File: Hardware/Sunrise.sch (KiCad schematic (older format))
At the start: 8 parts, among them U1 LM3401, U2 HC-06

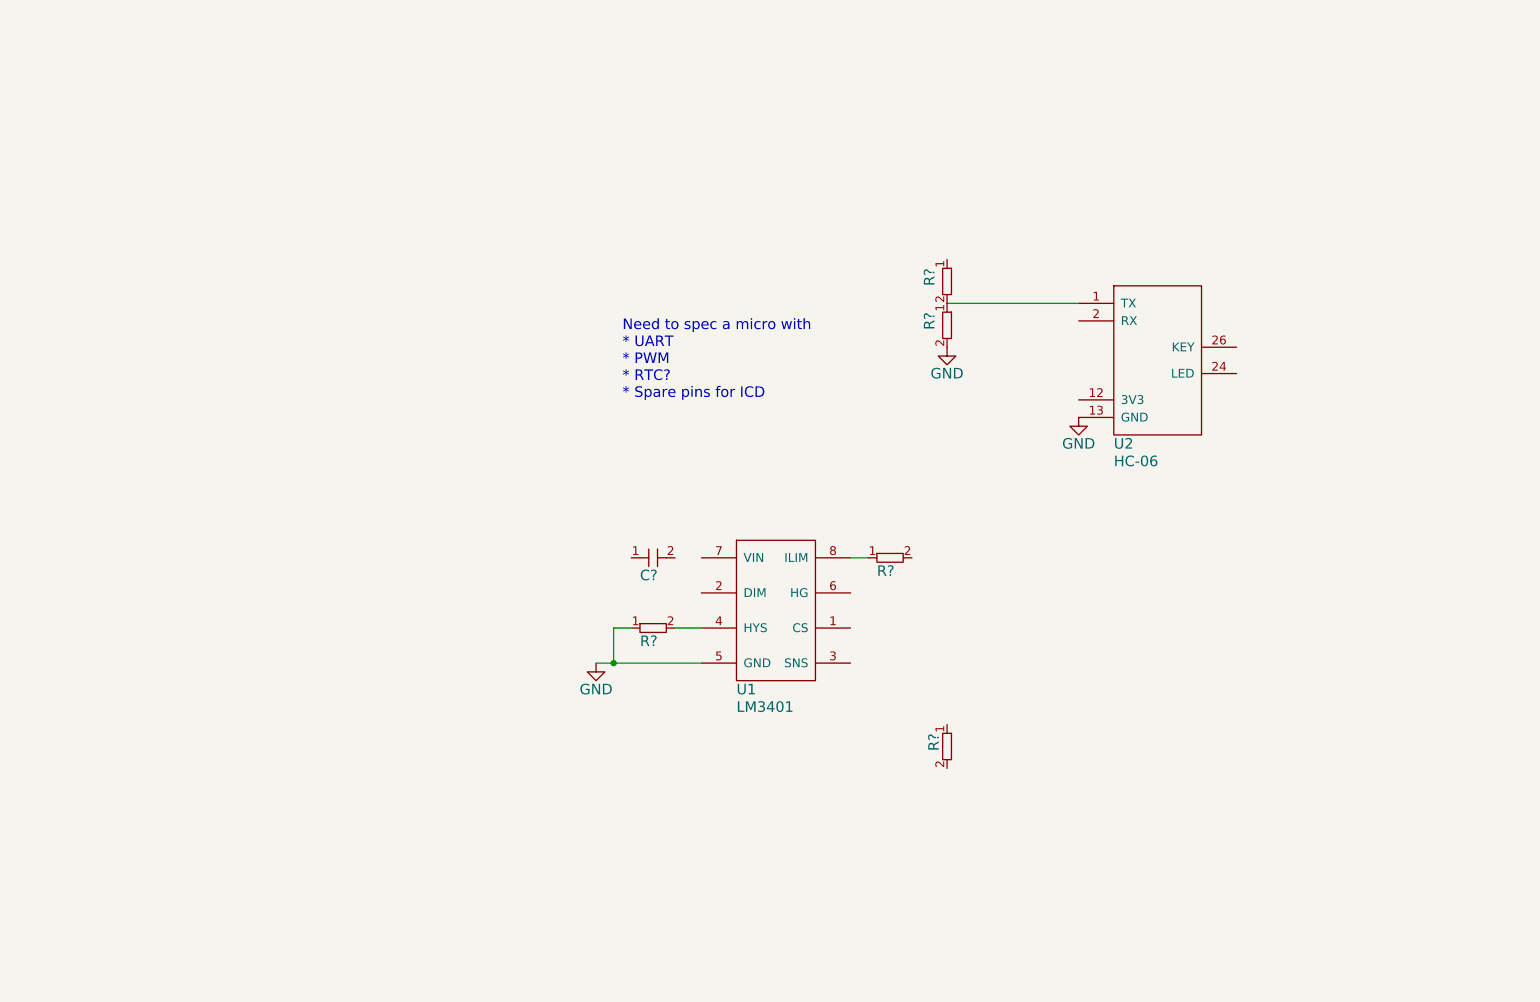
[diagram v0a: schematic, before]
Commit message: LED part of schematic drawn
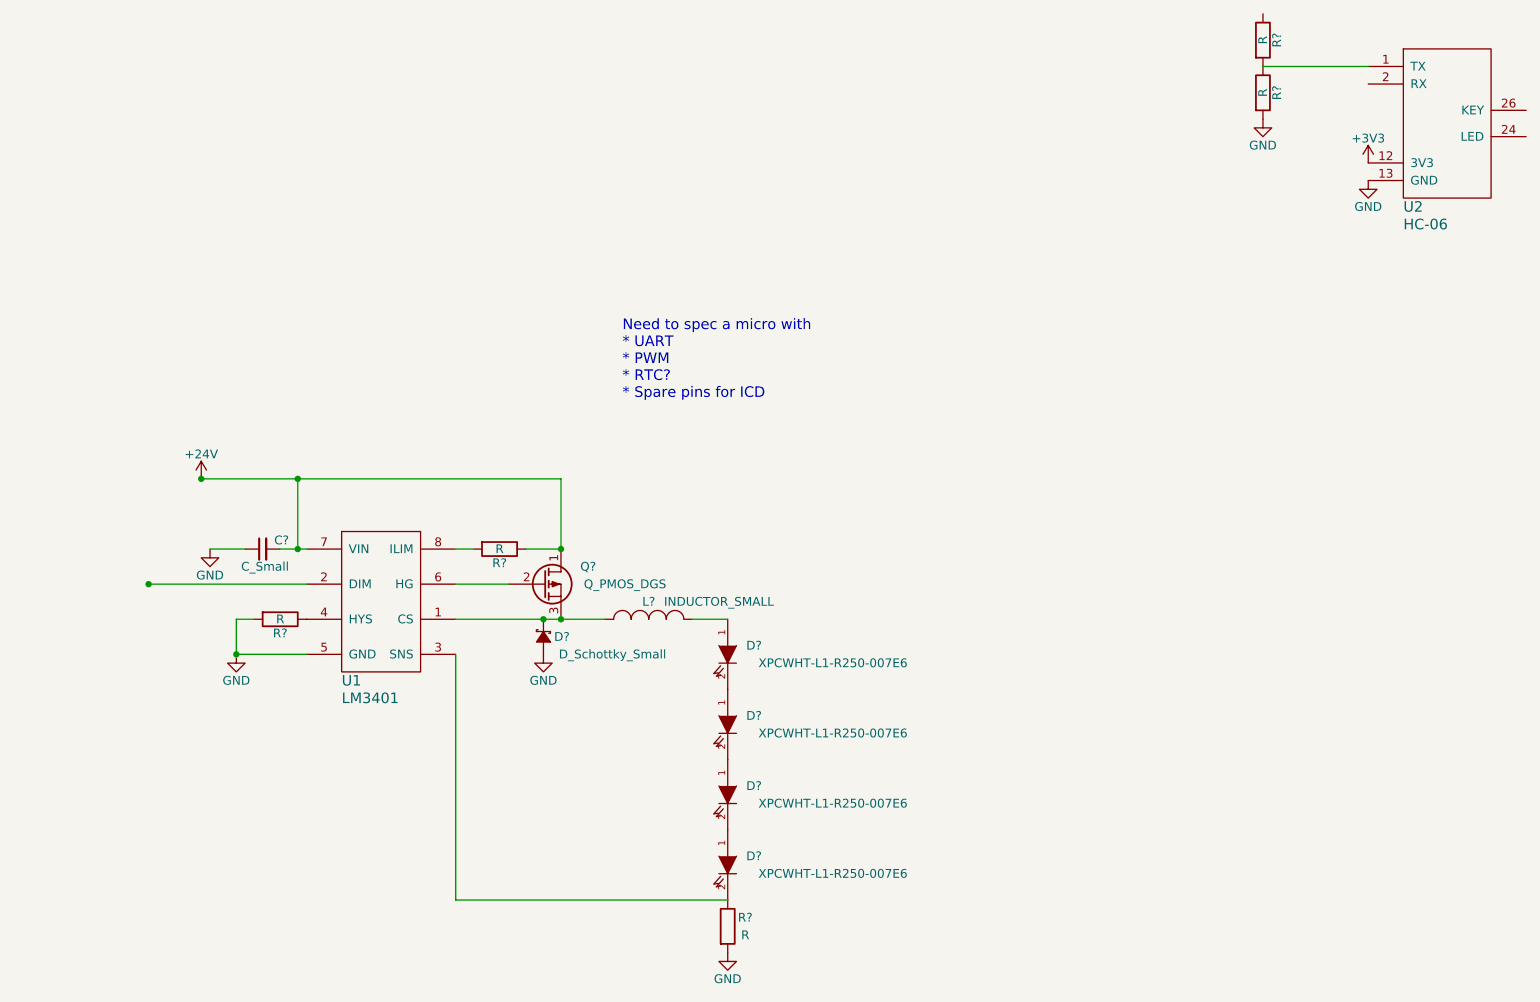
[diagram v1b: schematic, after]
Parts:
- removed C?: Cap, symbol Cap
- removed R? (x5): Resistor, symbol Resistor
- added C?: C_Small, symbol C_Small
- added D?: D_Schottky_Small, symbol D_Schottky_Small
- added D? (x4): XPCWHT-L1-R250-007E6, symbol LED
- added L?: INDUCTOR_SMALL, symbol INDUCTOR_SMALL
- added Q?: Q_PMOS_DGS, symbol Q_PMOS_DGS
- added R? (x5): R, symbol R
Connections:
- net GND: now also C?.1, D?.1 (A), R?.2, R?.2, R?.2
- net at U2.1 (TX): now also R?.1, R?.2
- net +3V3: now reaches U2.12 (3V3)
- net at U1.1 (CS): now also D?.2 (C), L?.1, Q?.3 (S)
- net at U1.3 (SNS): now also D?.2 (K), R?.1
- net at U1.4 (HYS): now also R?.1
- net at U1.6 (HG): now also Q?.2 (G)
- net +24V: now reaches U1.7 (VIN)
- net +24V: now also C?.2, Q?.1 (D), R?.1
- net at U1.8 (ILIM): now also R?.2
- new net: D?.1 (A), L?.2
- new net: D?.1 (A), D?.2 (K) (x3)
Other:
- moved on the sheet: U1, U2

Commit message: Added detail to schematic. Started LED driver calcs in python
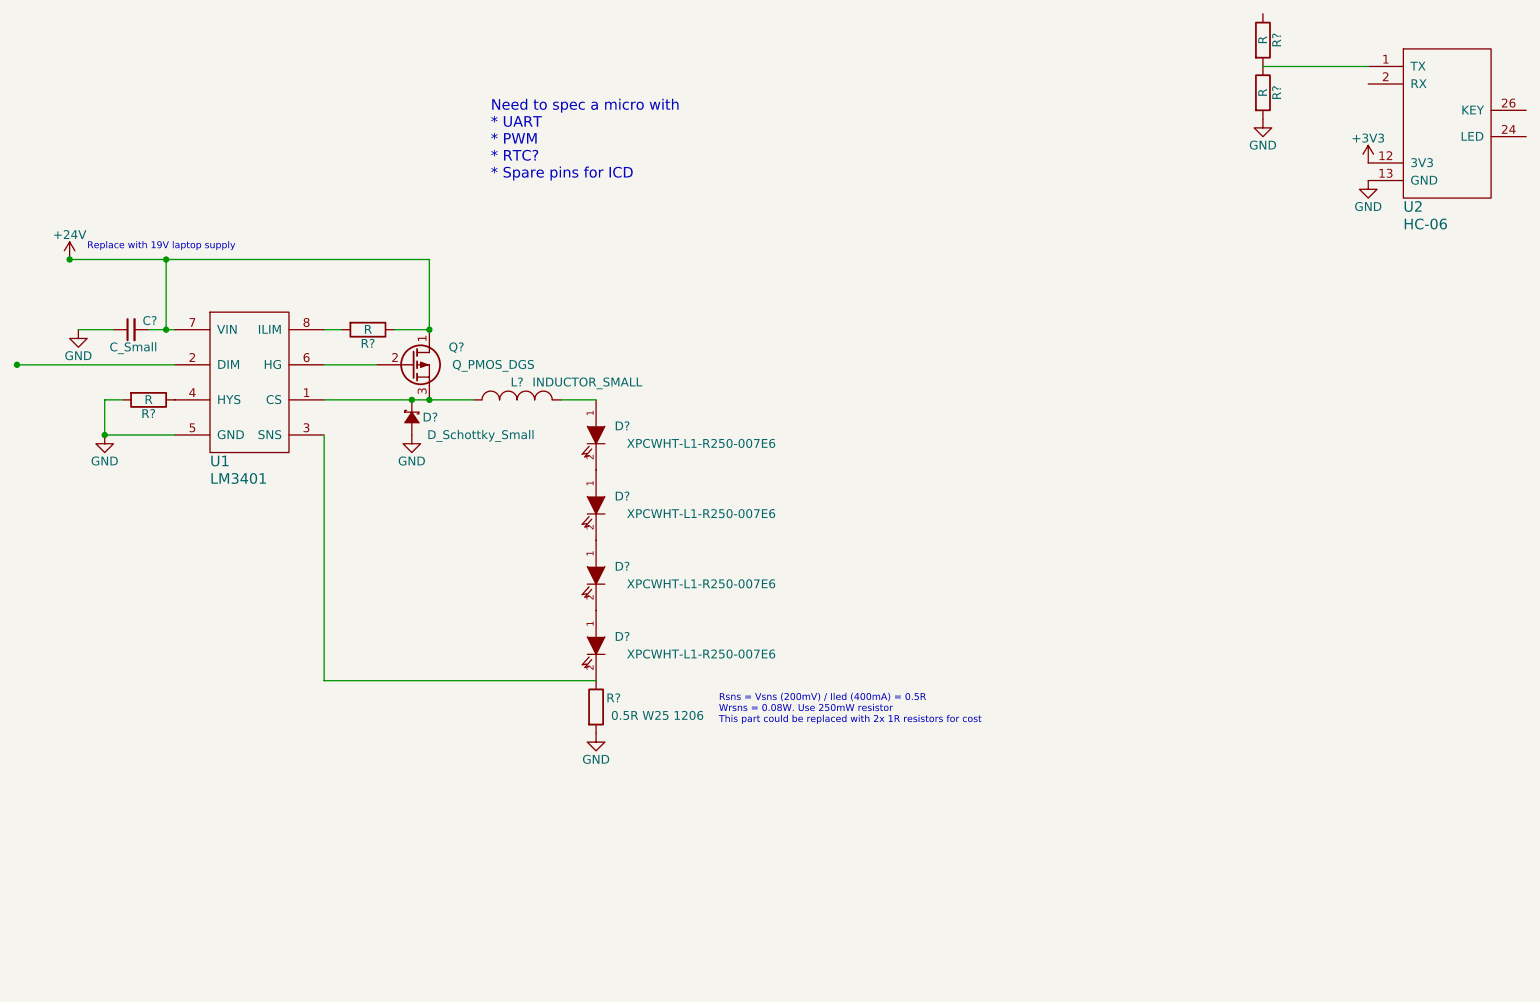
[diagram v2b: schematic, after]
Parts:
- R?: value R -> 0.5R W25 1206
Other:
- note added: "Replace with 19V laptop supply"
- note added: "Rsns = Vsns (200mV) / Iled (400mA) = 0.5R\nWrsns = 0.08W. Use 250mW resistor\nThis part could be replaced with 2x 1R resistors for cost"
- moved on the sheet: C?, D?, L?, Q?, R?, U1
